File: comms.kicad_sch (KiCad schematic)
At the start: 4 parts

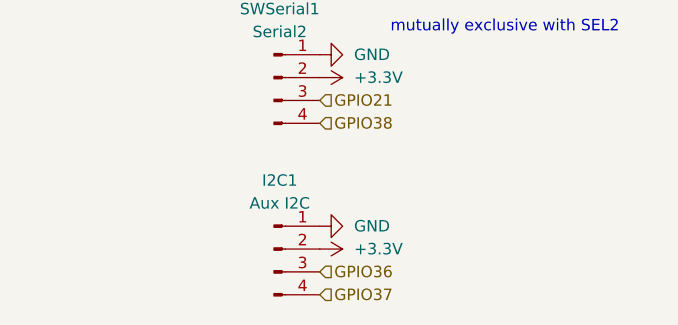
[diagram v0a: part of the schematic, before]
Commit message: Remapped GPIOs for clean routing
This updates the GPIO table so that the traces and vias are far cleaner. Slight repositioning of some pins to account for that. Rebuilt all gerbers and necessary stuff.
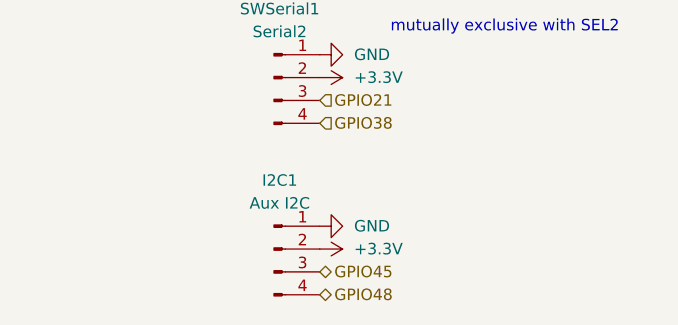
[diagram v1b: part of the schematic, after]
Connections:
- net GPIO36 renamed GPIO45
- net GPIO37 renamed GPIO48
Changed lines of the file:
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@@
 		)
 	)
-	(hierarchical_label "GPIO36"
-		(shape input)
+	(hierarchical_label "GPIO45"
+		(shape bidirectional)
 		(at 59.69 109.22 0)
 		(effects
@@
 		)
 	)
-	(hierarchical_label "GPIO37"
-		(shape input)
+	(hierarchical_label "GPIO48"
+		(shape bidirectional)
 		(at 59.69 111.76 0)
 		(effects

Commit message: Updated to v1.1 to fix issues
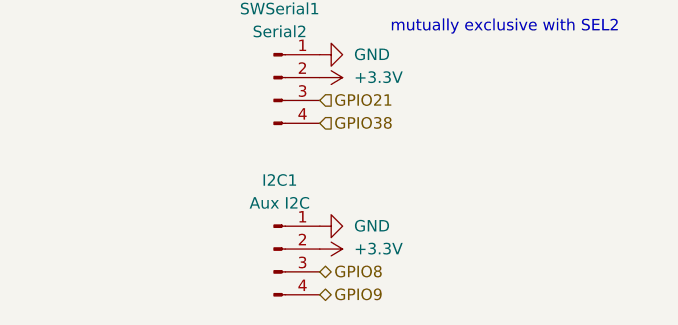
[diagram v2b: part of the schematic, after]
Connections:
- net GPIO45 renamed GPIO8
- net GPIO48 renamed GPIO9
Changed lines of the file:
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@@
 		)
 	)
-	(hierarchical_label "GPIO45"
+	(hierarchical_label "GPIO8"
 		(shape bidirectional)
 		(at 59.69 109.22 0)
@@
 		)
 	)
-	(hierarchical_label "GPIO48"
+	(hierarchical_label "GPIO9"
 		(shape bidirectional)
 		(at 59.69 111.76 0)
